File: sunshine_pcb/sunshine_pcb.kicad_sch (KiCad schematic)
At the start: 56 parts, among them J1 Soldered, J2 Conn_01x03, J5 VerticalUSB, Q1 AO3401A, SW1 Fingertech, U1 ESP32-S3-WROOM-1, U2 SPX1117M3, U3 LIS3MDL, U4 ADXL375, U8 USBLC6-2P6

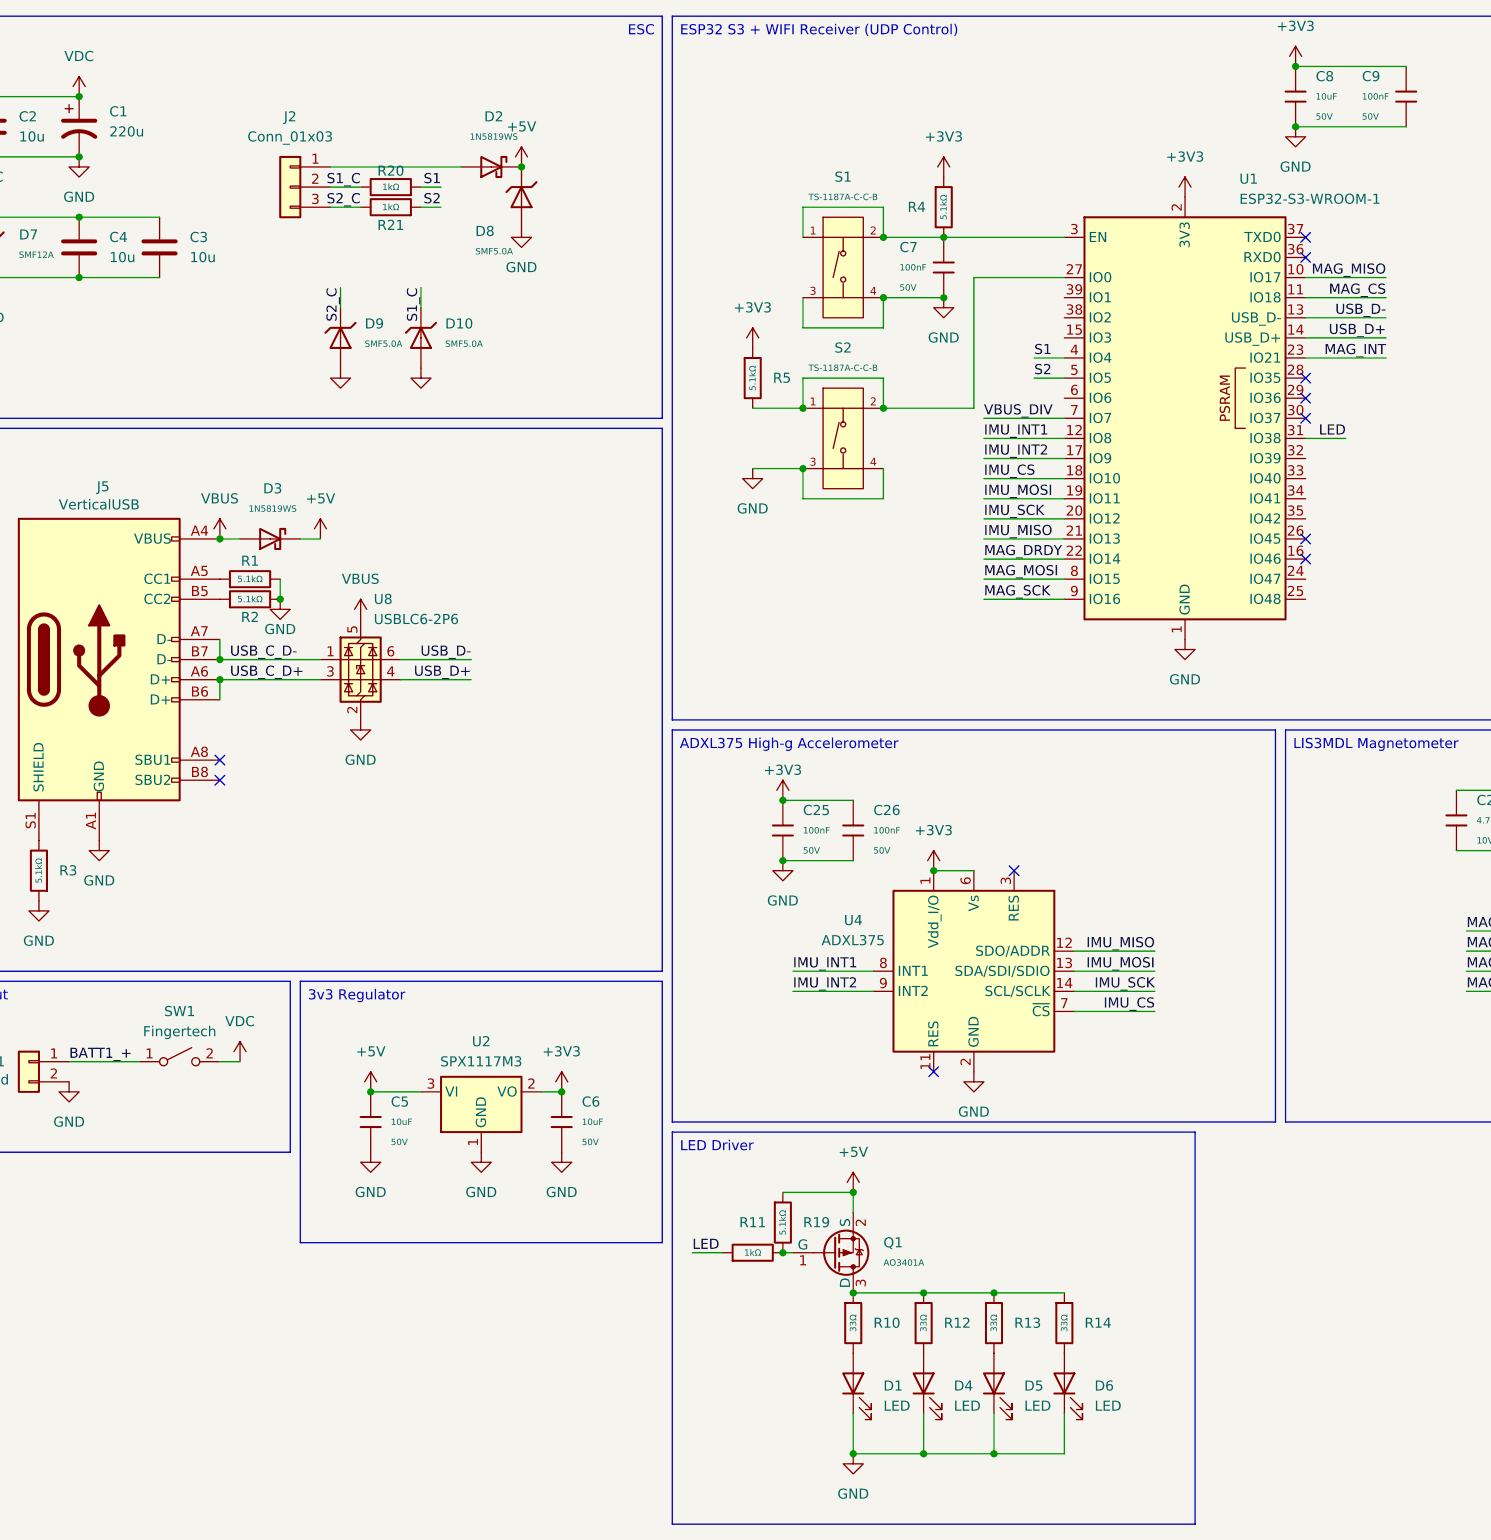
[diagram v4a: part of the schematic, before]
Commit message: Re-layout board for ESP32
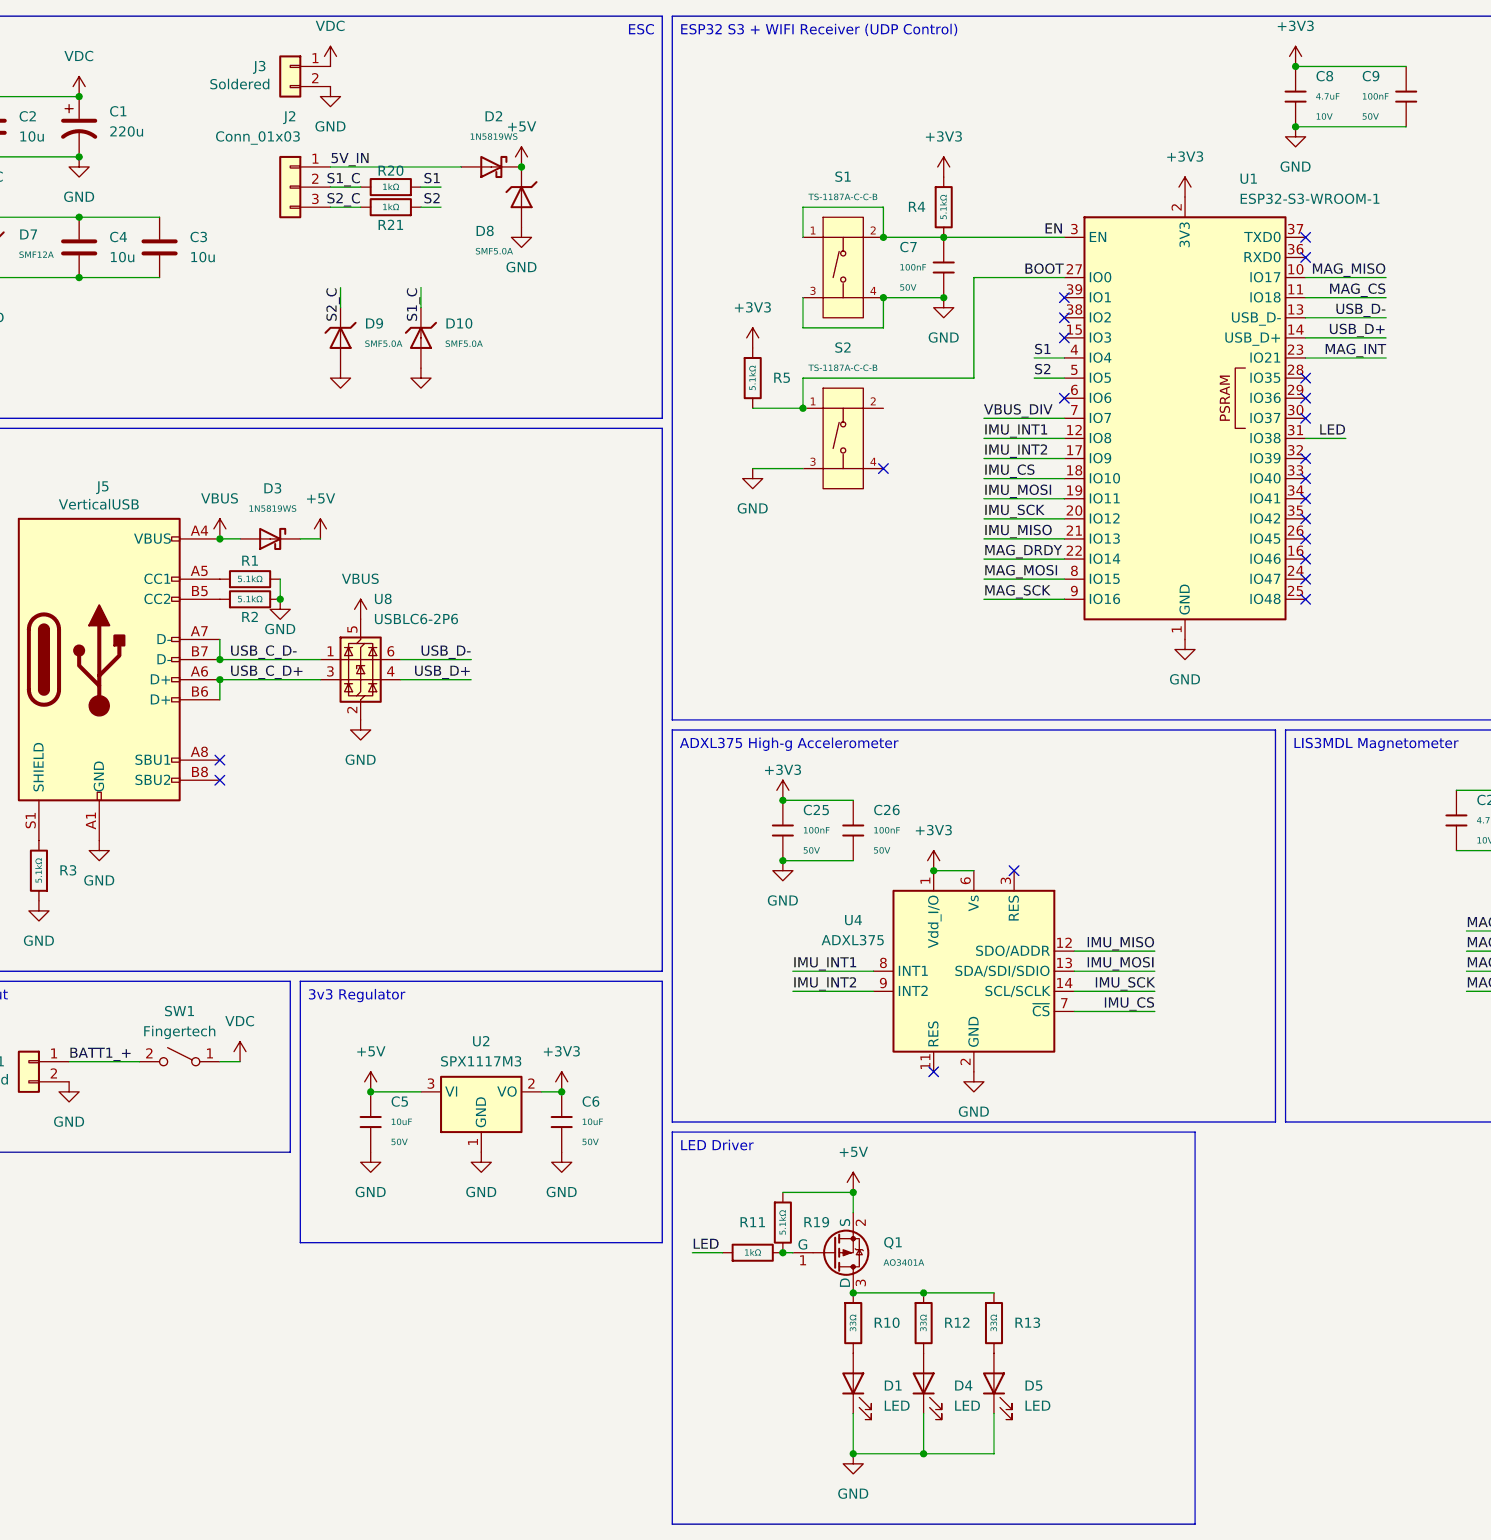
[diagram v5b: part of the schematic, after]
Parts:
- removed C8: 10uF, PCM_JLCPCB:C_0805, symbol PCM_JLCPCB-Capacitors:0805,10uF,(2)
- removed D6: LED, LED_SMD:LED_PLCC_2835, symbol Device:LED
- removed R14: 33Ω, PCM_JLCPCB:R_0805, symbol PCM_JLCPCB-Resistors:0805,33Ω
- added C8: 4.7uF, PCM_JLCPCB:C_0402, symbol PCM_JLCPCB-Capacitors:0402,4.7uF
- added J3: Soldered, Connector_Wire:SolderWire-0.75sqmm_1x02_P4.8mm_D1.25mm_OD2.3mm_Relief, symbol Connector_Generic:Conn_01x02
- J2: footprint Connector_Wire:SolderWire-0.25sqmm_1x03_P4.5mm_D0.65mm_OD2mm -> Connector_Wire:SolderWire-0.25sqmm_1x03_P4.2mm_D0.65mm_OD1.7mm
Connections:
- net +3V3: now also C8.1
- net BATT1_+: now also SW1.2 (B); no longer SW1.1 (A)
- net GND: now also C8.2, J3.2 (Pin_2); no longer S2.4 (D)
- net VDC: now also SW1.1 (A), J3.1 (Pin_1); no longer SW1.2 (B)
- net 5V_IN: now reaches D2.2, J2.1 (Pin_1)
- net EN: now reaches C7.1, R4.2, S1.1 (A), S1.2 (B), U1.3 (EN)
- net BOOT: now reaches R5.2, S2.1 (A), U1.27 (IO0)
- net BOOT: no longer S2.2 (B)
- no-connect marks 11 -> 22

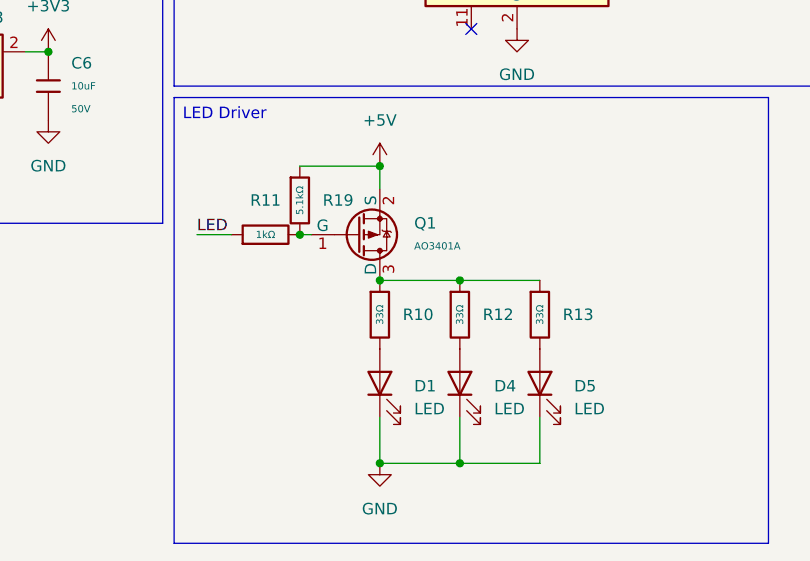
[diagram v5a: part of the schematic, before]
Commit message: Fix issue with mosfet
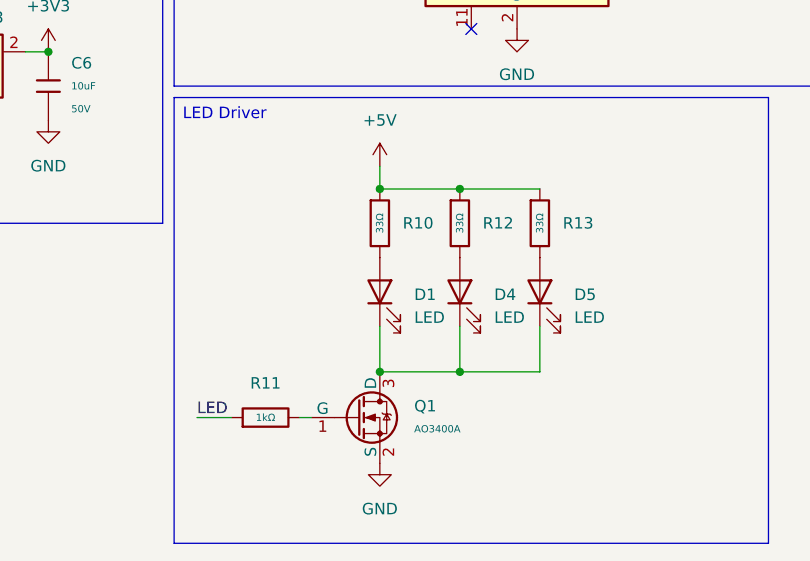
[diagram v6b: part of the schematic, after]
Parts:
- removed Q1: AO3401A, PCM_JLCPCB:Q_SOT-23, symbol PCM_JLCPCB-Transistors:PMOS,AO3401A
- removed R19: 5.1kΩ, PCM_JLCPCB:R_0402, symbol PCM_JLCPCB-Resistors:0402,5.1kΩ
- added Q1: AO3400A, PCM_JLCPCB:Q_SOT-23, symbol PCM_JLCPCB-Transistors:NMOS,AO3400A
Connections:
- net +5V: now also R10.1, R12.1, R13.1
- net GND: now also Q1.2 (S); no longer D1.1 (K), D4.1 (K), D5.1 (K)
- net at R11.2: now also Q1.1 (G)
- new net: D1.1 (K), D4.1 (K), D5.1 (K), Q1.3 (D)
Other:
- moved on the sheet: D1, D4, D5, R10, R11, R12, R13

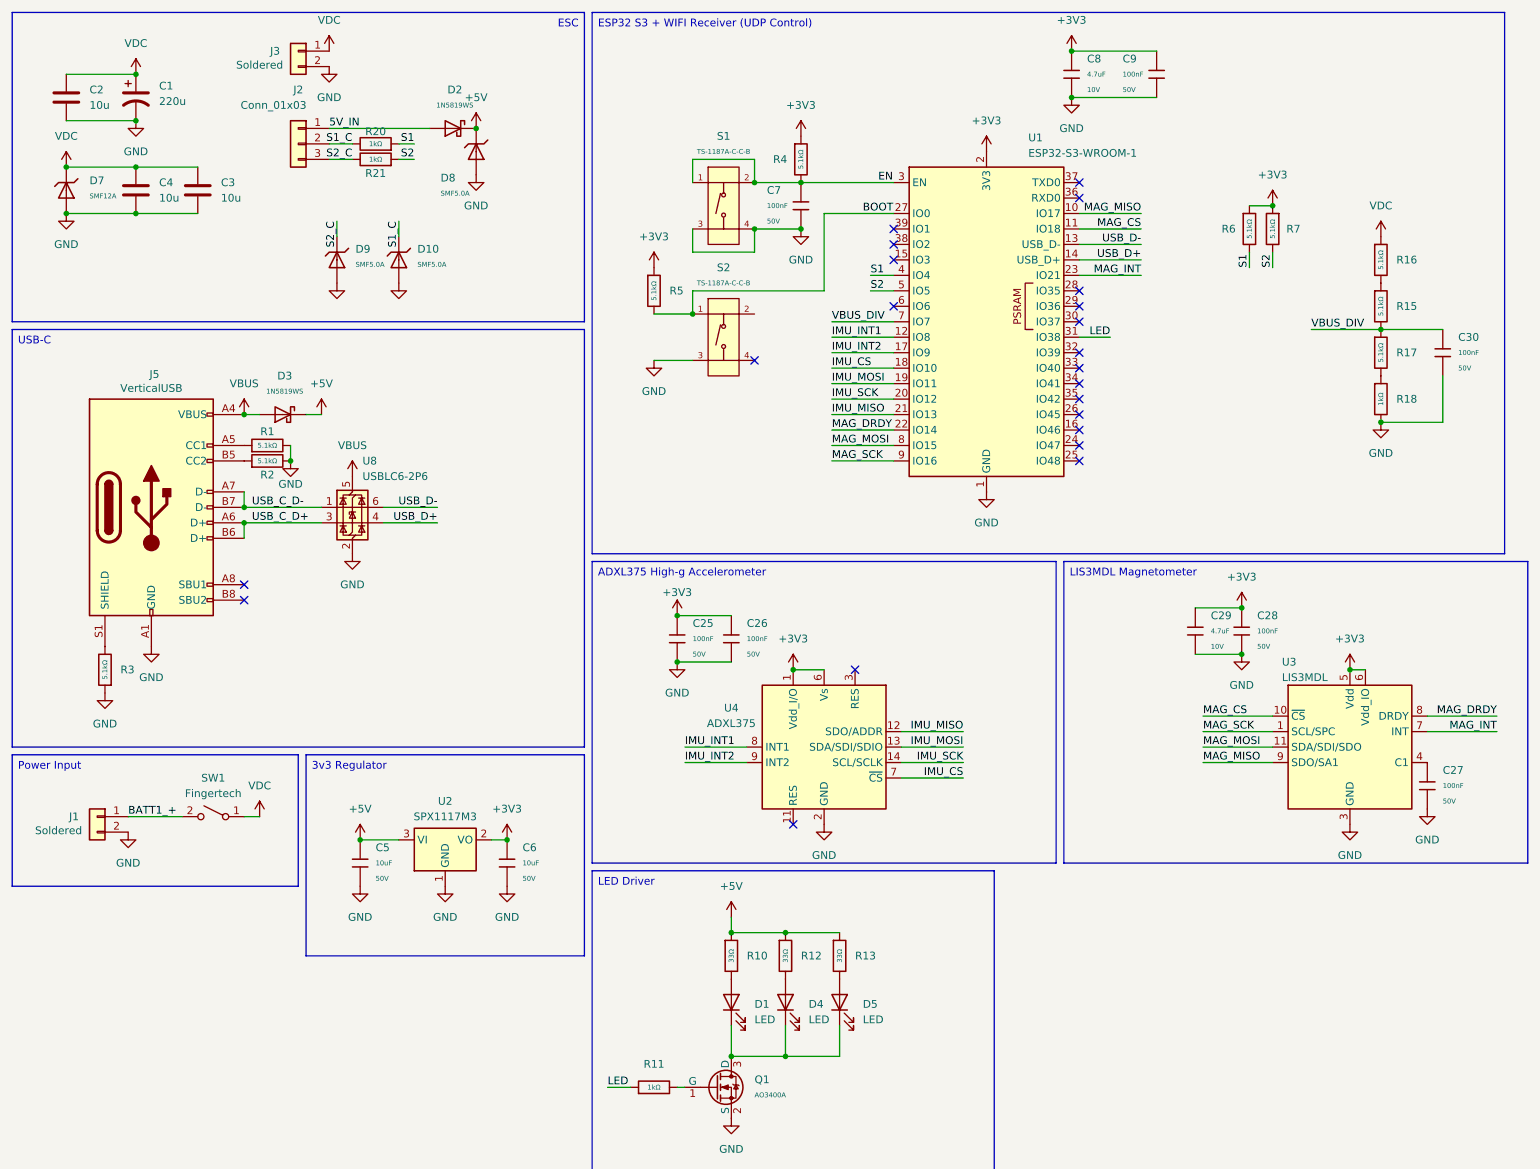
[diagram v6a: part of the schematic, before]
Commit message: Re-design PCB to not interact with VDC
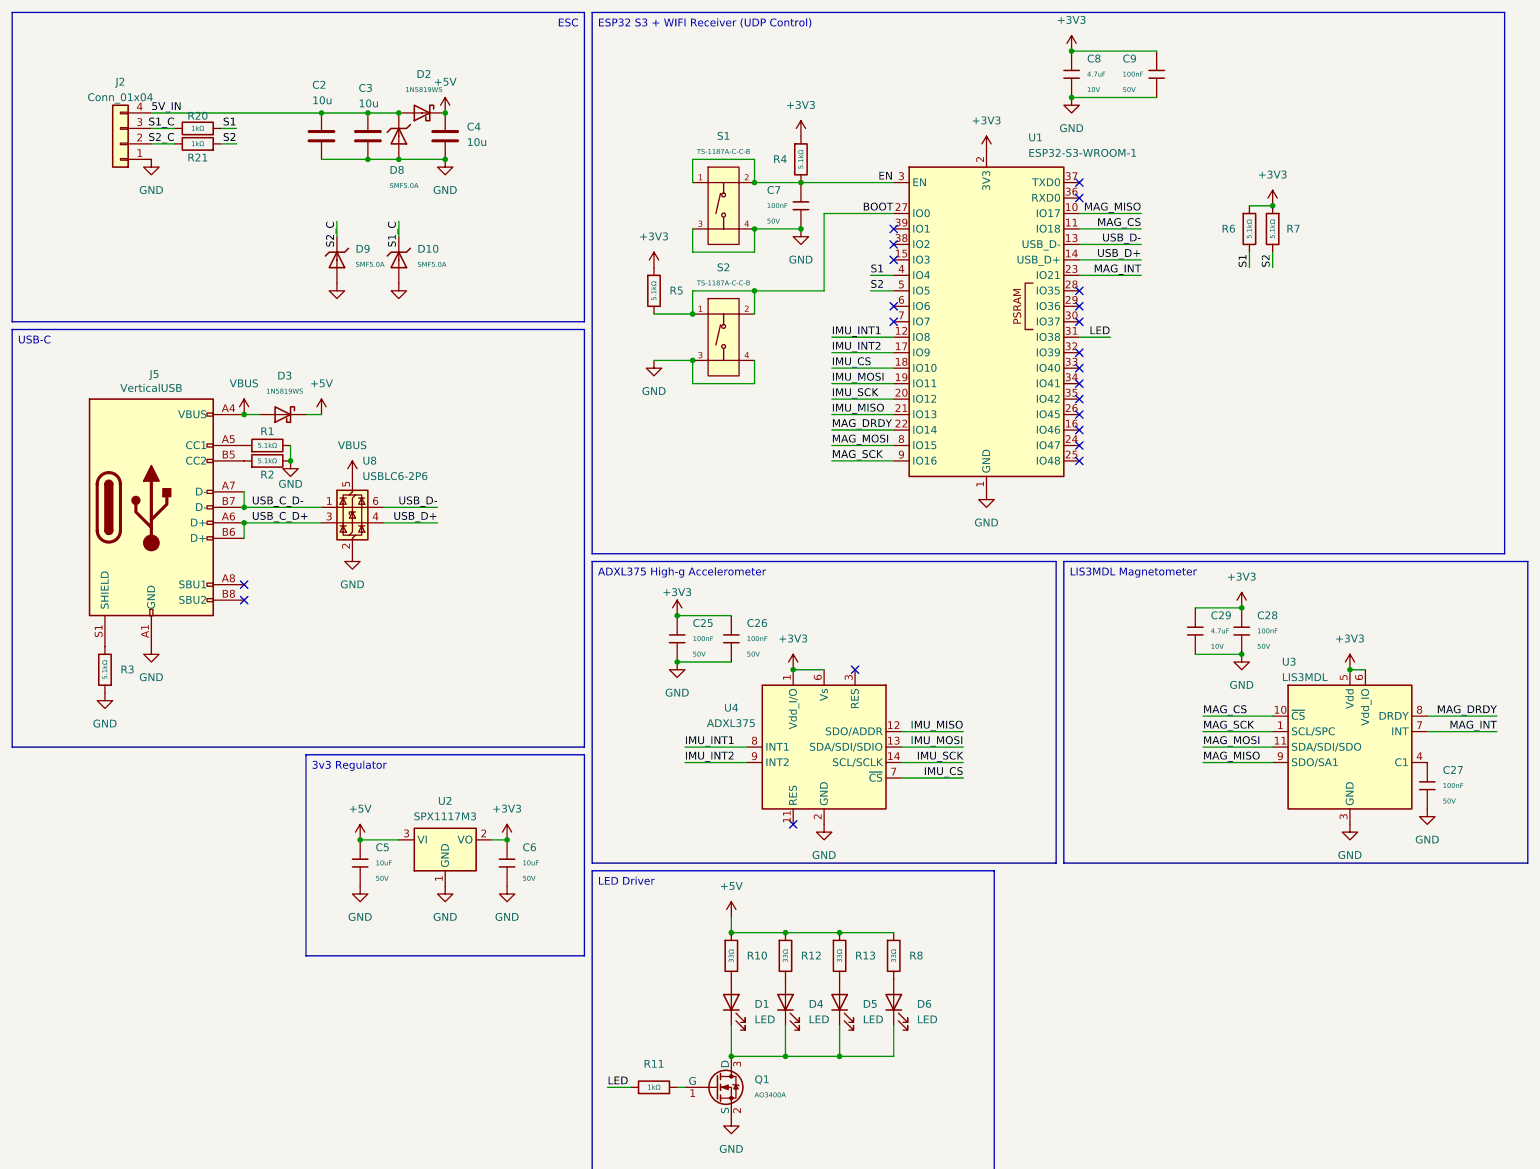
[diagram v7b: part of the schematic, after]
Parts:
- removed C1: 220u, Capacitor_THT:CP_Radial_D6.3mm_P2.50mm, symbol Device:C_Polarized_US
- removed C30: 100nF, PCM_JLCPCB:C_0402, symbol PCM_JLCPCB-Capacitors:0402,100nF,(2)
- removed D7: SMF12A, PCM_JLCPCB:D_SOD-123FL, symbol PCM_JLCPCB-Diodes:TVS-Uni,SMF12A
- removed J1, J3: Soldered, Connector_Wire:SolderWire-0.75sqmm_1x02_P4.8mm_D1.25mm_OD2.3mm_Relief, symbol Connector_Generic:Conn_01x02
- removed J2: Conn_01x03, Connector_Wire:SolderWire-0.25sqmm_1x03_P4.2mm_D0.65mm_OD1.7mm, symbol Connector_Generic:Conn_01x03
- removed R15, R16, R17: 5.1kΩ, PCM_JLCPCB:R_0402, symbol PCM_JLCPCB-Resistors:0402,5.1kΩ
- removed R18: 1kΩ, PCM_JLCPCB:R_0402, symbol PCM_JLCPCB-Resistors:0402,1kΩ
- removed SW1: Fingertech, custom:FingertechSwitch, symbol Switch:SW_SPST
- added D6: LED, LED_SMD:LED_PLCC_2835, symbol Device:LED
- added J2: Conn_01x04, Connector_Molex:Molex_Micro-Fit_3.0_43045-0400_2x02_P3.00mm_Horizontal, symbol Connector_Generic:Conn_01x04
- added R8: 33Ω, PCM_JLCPCB:R_0805, symbol PCM_JLCPCB-Resistors:0805,33Ω
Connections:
- net +5V: now also C4.1, R8.1; no longer D8.1
- net 5V_IN: now also C2.1, C3.1, D8.1, J2.4 (Pin_4)
- net BOOT: now also S2.2 (B)
- net GND: now also S2.4 (D), J2.1 (Pin_1)
- net S1_C: now also J2.3 (Pin_3)
- net S2_C: now also J2.2 (Pin_2)
- net at D1.1 (K), D4.1 (K), D5.1 (K)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: now also D6.1 (K)
- net VBUS_DIV: no longer names the net of U1.7 (IO7)
- removed net VDC: C2.1, C3.1, C4.1
- new net: D6.2 (A), R8.2
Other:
- moved on the sheet: C2, C3, C4, D2, D8, R20, R21

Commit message: Change connector to be soldered
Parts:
- J2: footprint Connector_Molex:Molex_Micro-Fit_3.0_43045-0400_2x02_P3.00mm_Horizontal -> custom:SolderConnector4P
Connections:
- net S1: now also R21.1; no longer R20.1
- net S1_C: now also J2.2 (Pin_2), R21.2; no longer J2.3 (Pin_3), R20.2
- net S2: now also R20.1; no longer R21.1
- net S2_C: now also J2.3 (Pin_3), R20.2; no longer J2.2 (Pin_2), R21.2
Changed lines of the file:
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@@
 		)
 	)
-	(label "S2"
+	(label "S1"
 		(at 50.8 35.56 180)
 		(effects
@@
 		)
 	)
-	(label "S2_C"
+	(label "S1_C"
 		(at 40.64 35.56 180)
 		(effects
@@
 		)
 	)
-	(label "S1"
+	(label "S2"
 		(at 50.8 33.02 180)
 		(effects
@@
 		)
 	)
-	(label "S1_C"
+	(label "S2_C"
 		(at 40.64 33.02 180)
 		(effects
@@
 			)
 		)
-		(property "Footprint" "Connector_Molex:Molex_Micro-Fit_3.0_43045-0400_2x02_P3.00mm_Horizontal"
+		(property "Footprint" "custom:SolderConnector4P"
 			(at 31.75 35.56 0)
 			(effects
